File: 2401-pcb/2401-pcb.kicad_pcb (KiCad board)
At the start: 2 copper layers, 140 x 30 mm, 87 parts, among them J1 Load Cell, J2 Conn_ARM_JTAG_SWD_10, J3 Conn_01x04_Male, Q1 SFH3710, Q2 SFH3710, SW1 SW_SPDT, U1 LIS3DH, U10 MCP6001U, U11 MCP6001U, U2 VL6180X, U3 INA126, U4 MCP6001U, U5 DPS422, U6 MCP6001U, U7 TLV70228_SOT23-5, U8 STM32G070KBT6, U9 AT25SF641-SUB-T

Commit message: PCB: schematics & layout complete [Checklist PASS]
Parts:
- added LOGO1: LOGO, Jitter_Logos:Jitter, F.Cu at (223.5, 126.2)
- added LOGO2: LOGO, Jitter_Logos:Symbol_Jitter-Icon_CopperAndSilkScreenTop, F.Cu at (141.8, 117.2)
- added LOGO3: LOGO, Jitter_Logos:Jitter, B.Cu at (227.0, 115.0)
- added LOGO4: LOGO, Logo:GND, B.Cu at (168.3, 122.7)
- added MB1: Mousebite, Jitter_Footprints:MouseBite_3.5mmx2.2mm_breakaway, F.Cu at (118.0, 100.0)
- added MB2: Mousebite, Jitter_Footprints:MouseBite_3.5mmx2.2mm_breakaway, F.Cu at (219.0, 100.0)
- added MB3: Mousebite, Jitter_Footprints:MouseBite_3.5mmx2.2mm_breakaway, F.Cu at (121.3, 130.0)
- added MB4: Mousebite, Jitter_Footprints:MouseBite_3.5mmx2.2mm_breakaway, F.Cu at (222.3, 130.0)
- added TH1: ToolingHole, Jitter_Footprints:Tooling_hole_4mm_4.04mm_paste, F.Cu at (220.0, 95.0)
- added TH2: ToolingHole, Jitter_Footprints:Tooling_hole_4mm_4.04mm_paste, F.Cu at (220.0, 135.0)
- added TH3: ToolingHole, Jitter_Footprints:Tooling_hole_4mm_4.04mm_paste, F.Cu at (120.0, 135.0)
- added TH4: ToolingHole, Jitter_Footprints:Tooling_hole_4mm_4.04mm_paste, F.Cu at (120.0, 95.0)
- TP14, TP17: footprint TestPoint:TestPoint_THTPad_D1.0mm_Drill0.5mm -> TestPoint:TestPoint_Pad_D1.0mm
- moved D1 0.15 mm to (132.8, 123.4)
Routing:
- net GND: track 95.1 -> 93.4 mm
- net /D1_V+: track 24.8 -> 25.7 mm
- net /load_cell: track 42.6 -> 43.5 mm
- net /SWDIO: track 15.2 -> 14.5 mm
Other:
- board size 140 x 30 mm -> 140 x 50 mm
- board text added: "2401-pcb1-1"
- board text added: "Debug (SWD)"
- board text added: "GND"
- board text added: "Made in Delft"
- board text added: "Rx"
- board text added: "Tx"
- board text added: "VCC"

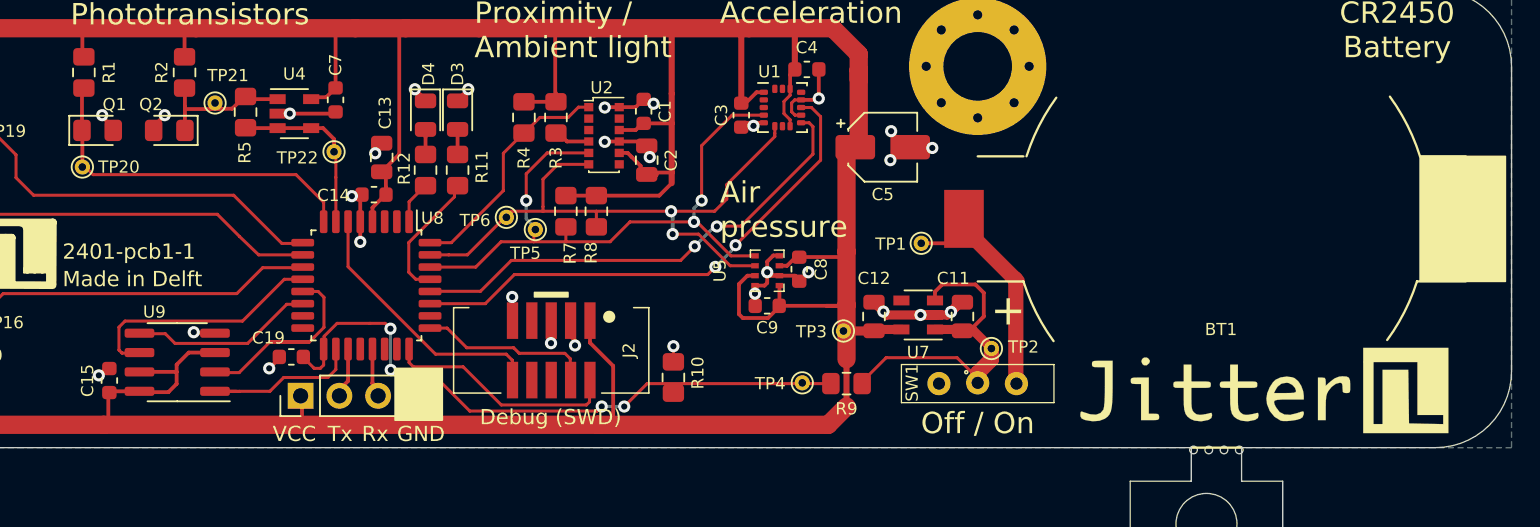
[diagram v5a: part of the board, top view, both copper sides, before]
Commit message: PCB/Schematic bugfix: add NRST capacitor, update air pressure symbol
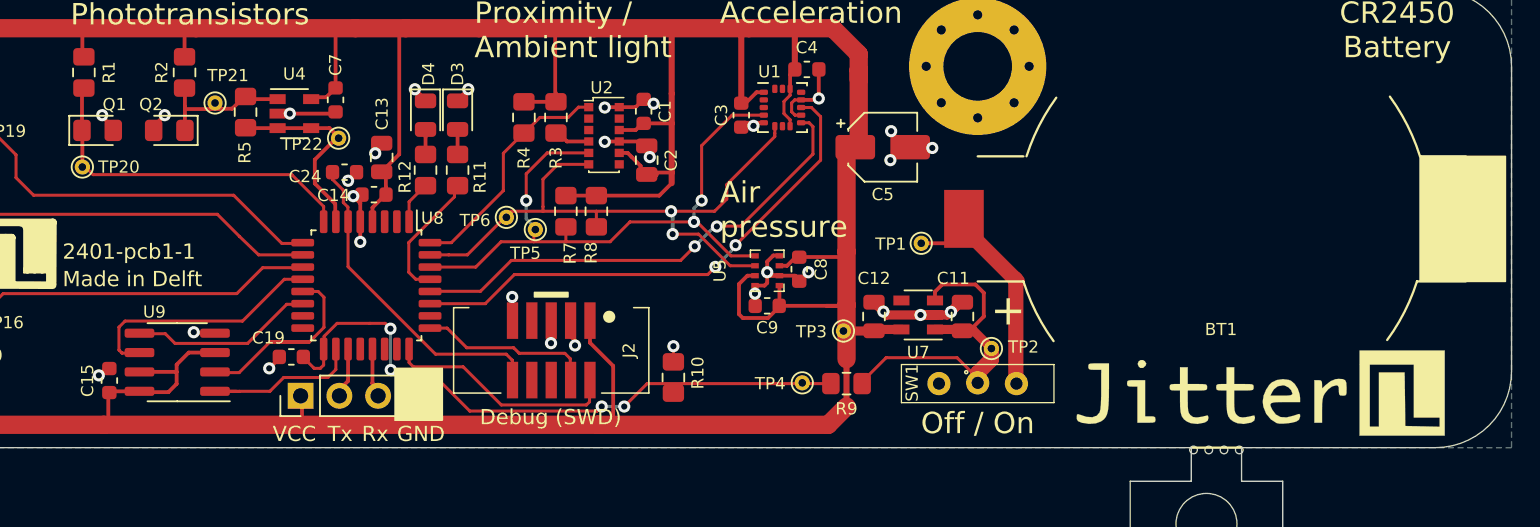
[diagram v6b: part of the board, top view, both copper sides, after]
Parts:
- added C24: 100nF, Capacitor_SMD:C_0603_1608Metric, F.Cu at (163.5, 111.9)
- moved TP22 0.94 mm to (163.1, 109.7)
- moved LOGO1 0.29 mm to (223.3, 126.4)
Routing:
- net /~RST: track 17.6 -> 21.3 mm
- net /photo_transistor_2: track 11.6 -> 13.4 mm
- net GND: track 93.4 -> 94.3 mm, vias 53 -> 54
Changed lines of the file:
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@@
     (thickness 1.6)
     (drawings 133)
-    (tracks 693)
+    (tracks 704)
     (zones 0)
-    (modules 99)
+    (modules 100)
     (nets 41)
   )
@@
     (add_net "Net-(D3-Pad2)")
     (add_net "Net-(D4-Pad2)")
+    (add_net "Net-(J2-Pad6)")
+    (add_net "Net-(J2-Pad7)")
+    (add_net "Net-(J2-Pad8)")
     (add_net "Net-(Q2-Pad1)")
     (add_net "Net-(R3-Pad2)")
+    (add_net "Net-(RV1-Pad1)")
     (add_net "Net-(RV1-Pad2)")
     (add_net "Net-(RV1-Pad3)")
+    (add_net "Net-(SW1-Pad3)")
+    (add_net "Net-(U1-Pad13)")
+    (add_net "Net-(U1-Pad15)")
+    (add_net "Net-(U1-Pad16)")
+    (add_net "Net-(U1-Pad2)")
+    (add_net "Net-(U1-Pad3)")
+    (add_net "Net-(U1-Pad7)")
+    (add_net "Net-(U7-Pad4)")
+    (add_net "Net-(U8-Pad15)")
+    (add_net "Net-(U8-Pad16)")
+    (add_net "Net-(U8-Pad2)")
+    (add_net "Net-(U8-Pad20)")
+    (add_net "Net-(U8-Pad22)")
+    (add_net "Net-(U8-Pad23)")
+    (add_net "Net-(U8-Pad26)")
+    (add_net "Net-(U8-Pad3)")
     (add_net Vbatt)
   )
+  (module Capacitor_SMD:C_0603_1608Metric (layer F.Cu)
+    (at 163.49 111.94)
+    (descr "Capacitor SMD 0603 (1608 Metric), square (rectangular) end terminal, IPC_7351 nominal, (Body size source: http://www.tortai-tech.com/upload/download/2011102023233369053.pdf), generated with kicad-footprint-generator")
+    (tags capacitor)
+    (attr smd)
+    (fp_text reference C24 (at -2.59 0.28) (layer F.SilkS)
+      (effects (font (size 0.8 0.8) (thickness 0.15)))
+    )
+    (fp_text value 100nF (at 0 1.43) (layer F.Fab)
+      (effects (font (size 1 1) (thickness 0.15)))
+    )
+    (fp_text user %R (at 0 0) (layer F.Fab)
+      (effects (font (size 0.4 0.4) (thickness 0.06)))
+    )
+    (fp_line (start 1.48 0.73) (end -1.48 0.73) (layer F.CrtYd) (width 0.05))
+    (fp_line (start 1.48 -0.73) (end 1.48 0.73) (layer F.CrtYd) (width 0.05))
+    (fp_line (start -1.48 -0.73) (end 1.48 -0.73) (layer F.CrtYd) (width 0.05))
+    (fp_line (start -1.48 0.73) (end -1.48 -0.73) (layer F.CrtYd) (width 0.05))
+    (fp_line (start -0.162779 0.51) (end 0.162779 0.51) (layer F.SilkS) (width 0.12))
+    (fp_line (start -0.162779 -0.51) (end 0.162779 -0.51) (layer F.SilkS) (width 0.12))
+    (fp_line (start 0.8 0.4) (end -0.8 0.4) (layer F.Fab) (width 0.1))
+    (fp_line (start 0.8 -0.4) (end 0.8 0.4) (layer F.Fab) (width 0.1))
+    (fp_line (start -0.8 -0.4) (end 0.8 -0.4) (layer F.Fab) (width 0.1))
+    (fp_line (start -0.8 0.4) (end -0.8 -0.4) (layer F.Fab) (width 0.1))
+    (pad 2 smd roundrect (at 0.7875 0) (size 0.875 0.95) (layers F.Cu F.Paste F.Mask) (roundrect_rratio 0.25)
+      (net 1 GND))
+    (pad 1 smd roundrect (at -0.7875 0) (size 0.875 0.95) (layers F.Cu F.Paste F.Mask) (roundrect_rratio 0.25)
+      (net 27 /~RST))
+    (model ${KISYS3DMOD}/Capacitor_SMD.3dshapes/C_0603_1608Metric.wrl
+      (at (xyz 0 0 0))
+      (scale (xyz 1 1 1))
+      (rotate (xyz 0 0 0))
+    )
+  )
   (module Jitter_Logos:Jitter (layer B.Cu)
     (at 227 115 270)
@@
   )
   (module Jitter_Logos:Jitter (layer F.Cu)
-    (at 223.5 126.25)
+    (at 223.26 126.42)
     (attr virtual)
     (fp_text reference LOGO1 (at 0 0) (layer F.SilkS) hide
@@
   )
   (module TestPoint:TestPoint_THTPad_D1.0mm_Drill0.5mm (layer F.Cu)
-    (at 162.8 110.6)
+    (at 163.1 109.71)
     (descr "THT pad as test Point, diameter 1.0mm, hole diameter 0.5mm")
     (tags "test point THT pad")
@@
     (tags capacitor)
     (attr smd)
-    (fp_text reference C13 (at 2.925 0.225 90) (layer F.SilkS)
+    (fp_text reference C13 (at 2.865 0.025 90) (layer F.SilkS)
       (effects (font (size 0.8 0.8) (thickness 0.15)))
     )
@@
     (tags "resistor handsolder")
     (attr smd)
-    (fp_text reference R12 (at 0.1 -1.4 90) (layer F.SilkS)
+    (fp_text reference R12 (at -0.45 -1.35 90) (layer F.SilkS)
       (effects (font (size 0.8 0.8) (thickness 0.15)))
     )
@@
     (tags "resistor handsolder")
     (attr smd)
-    (fp_text reference R11 (at 0.2 1.6 90) (layer F.SilkS)
+    (fp_text reference R11 (at -0.45 1.47 90) (layer F.SilkS)
       (effects (font (size 0.8 0.8) (thickness 0.15)))
     )
@@
   (segment (start 183.3 110.65) (end 183.5 110.85) (width 0.25) (layer F.Cu) (net 1))
   (via (at 183.75 107.45) (size 0.8) (drill 0.4) (layers F.Cu B.Cu) (net 1))
-  (segment (start 164.52 115.185) (end 164.52 113.41) (width 0.25) (layer F.Cu) (net 1))
-  (via (at 163.97 113.51) (size 0.8) (drill 0.4) (layers F.Cu B.Cu) (net 1))
-  (segment (start 164.52 113.41) (end 164.42 113.51) (width 0.25) (layer F.Cu) (net 1))
-  (segment (start 164.42 113.51) (end 163.97 113.51) (width 0.25) (layer F.Cu) (net 1))
   (segment (start 181.5 107.675) (end 180.575 107.675) (width 0.25) (layer F.Cu) (net 1))
   (via (at 180.55 107.7) (size 0.8) (drill 0.4) (layers F.Cu B.Cu) (net 1))
@@
   (segment (start 177.04 121.67) (end 177.04 123.135) (width 0.25) (layer F.Cu) (net 1))
   (segment (start 177.04 123.135) (end 177.025 123.15) (width 0.25) (layer F.Cu) (net 1))
+  (segment (start 164.2775 111.94) (end 164.2775 111.9425) (width 0.25) (layer F.Cu) (net 1))
+  (via (at 163.72 112.5) (size 0.8) (drill 0.4) (layers F.Cu B.Cu) (net 1))
+  (segment (start 164.2775 111.9425) (end 163.72 112.5) (width 0.25) (layer F.Cu) (net 1))
+  (segment (start 164.460009 113.909999) (end 164.06001 113.51) (width 0.25) (layer F.Cu) (net 1))
+  (segment (start 164.52 113.96999) (end 164.460009 113.909999) (width 0.25) (layer F.Cu) (net 1))
+  (via (at 164.06001 113.51) (size 0.8) (drill 0.4) (layers F.Cu B.Cu) (net 1))
+  (segment (start 164.52 115.185) (end 164.52 113.96999) (width 0.25) (layer F.Cu) (net 1))
+  (segment (start 164.52 113.96999) (end 164.52 113.37) (width 0.25) (layer F.Cu) (net 1))
   (segment (start 137.05 107.45) (end 137.05 105.8) (width 0.4) (layer F.Cu) (net 2))
   (segment (start 161.4 107.025) (end 161.325 107.1) (width 0.25) (layer F.Cu) (net 2))
@@
   (segment (start 146.275 106.525) (end 146.4 106.4) (width 0.25) (layer F.Cu) (net 5))
   (segment (start 146.3 111.6) (end 146.3 109.4) (width 0.25) (layer F.Cu) (net 5))
-  (segment (start 146.5 111.6) (end 146.3 111.6) (width 0.2) (layer F.Cu) (net 5))
   (segment (start 147 112.1) (end 146.5 111.6) (width 0.2) (layer F.Cu) (net 5))
-  (segment (start 160.31 112.1) (end 147 112.1) (width 0.2) (layer F.Cu) (net 5))
-  (segment (start 162.12 115.185) (end 162.12 113.91) (width 0.2) (layer F.Cu) (net 5))
-  (segment (start 162.12 113.91) (end 160.31 112.1) (width 0.2) (layer F.Cu) (net 5))
+  (segment (start 160.03 112.1) (end 147 112.1) (width 0.2) (layer F.Cu) (net 5))
+  (segment (start 146.5 111.6) (end 146.3 111.6) (width 0.2) (layer F.Cu) (net 5))
+  (segment (start 162.12 115.185) (end 162.12 114.19) (width 0.2) (layer F.Cu) (net 5))
+  (segment (start 162.12 114.19) (end 160.03 112.1) (width 0.2) (layer F.Cu) (net 5))
   (segment (start 161.3 109.05) (end 158.95 109.05) (width 0.25) (layer F.Cu) (net 6))
   (segment (start 159.1 109.05) (end 156.95 109.05) (width 0.25) (layer F.Cu) (net 6))
   (segment (start 162.8 109.77) (end 162.8 109.892894) (width 0.25) (layer F.Cu) (net 6))
-  (segment (start 161.3 109.05) (end 162.08 109.05) (width 0.25) (layer F.Cu) (net 6))
-  (segment (start 162.08 109.05) (end 162.8 109.77) (width 0.25) (layer F.Cu) (net 6))
-  (segment (start 162.8 109.892894) (end 162.8 110.6) (width 0.25) (layer F.Cu) (net 6))
-  (segment (start 162.92 115.185) (end 162.92 112.28) (width 0.2) (layer F.Cu) (net 6))
-  (segment (start 162.92 112.28) (end 162.92 110.67) (width 0.2) (layer F.Cu) (net 6))
+  (segment (start 162.88 114.02) (end 162.88 115.15) (width 0.25) (layer F.Cu) (net 6))
+  (segment (start 162.5 109.05) (end 163.11 109.66) (width 0.25) (layer F.Cu) (net 6))
+  (segment (start 161.3 109.05) (end 162.5 109.05) (width 0.25) (layer F.Cu) (net 6))
+  (segment (start 163 109.66) (end 161.54 111.12) (width 0.25) (layer F.Cu) (net 6))
+  (segment (start 161.54 111.12) (end 161.54 112.68) (width 0.25) (layer F.Cu) (net 6))
+  (segment (start 161.54 112.68) (end 162.88 114.02) (width 0.25) (layer F.Cu) (net 6))
+  (segment (start 163.11 109.66) (end 163 109.66) (width 0.25) (layer F.Cu) (net 6))
   (segment (start 137.05 122.25) (end 138.05 122.25) (width 0.25) (layer F.Cu) (net 7))
   (segment (start 138.05 122.25) (end 138.9 122.25) (width 0.25) (layer F.Cu) (net 7))
@@
   (segment (start 174.09 123.87) (end 169.453944 123.87) (width 0.2) (layer F.Cu) (net 27))
   (segment (start 174.49 124.27) (end 174.09 123.87) (width 0.2) (layer F.Cu) (net 27))
+  (segment (start 163.41 113.93) (end 163.71 114.23) (width 0.2) (layer F.Cu) (net 27))
+  (segment (start 163.41 113.1225) (end 163.41 113.93) (width 0.2) (layer F.Cu) (net 27))
+  (segment (start 162.7025 111.94) (end 162.7025 112.415) (width 0.2) (layer F.Cu) (net 27))
+  (segment (start 163.71 114.23) (end 163.71 115.17) (width 0.2) (layer F.Cu) (net 27))
+  (segment (start 162.7025 112.415) (end 163.41 113.1225) (width 0.2) (layer F.Cu) (net 27))
   (segment (start 179.5 109.925) (end 178.075 109.925) (width 0.25) (layer F.Cu) (net 28))
   (segment (start 178.075 109.925) (end 177.6 109.45) (width 0.25) (layer F.Cu) (net 28))
